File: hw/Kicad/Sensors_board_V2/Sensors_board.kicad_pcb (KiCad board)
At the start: 2 copper layers, 70 x 100 mm, 17 parts, among them J1 SENSORES_LINEA, U1 CNY70, U2 CNY70, U3 CNY70, U4 CNY70, U5 CNY70, U6 CNY70, U7 4053

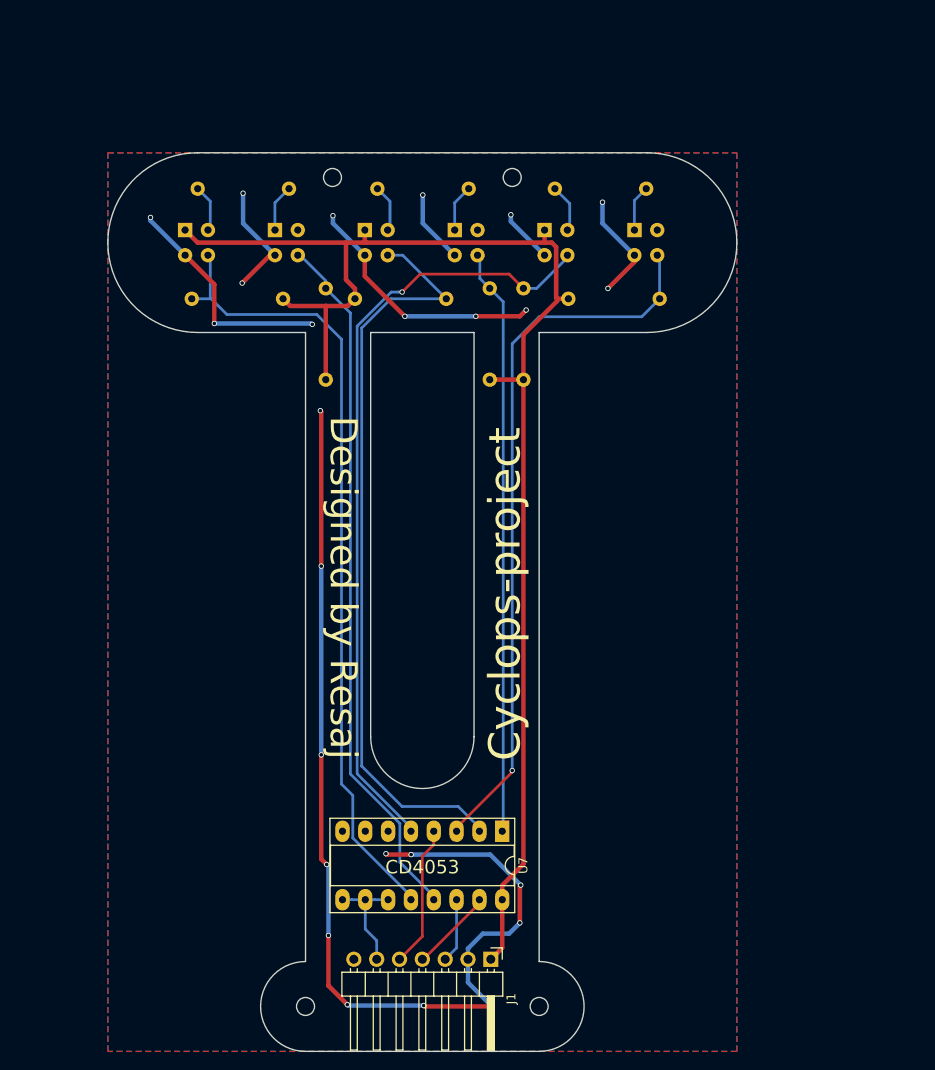
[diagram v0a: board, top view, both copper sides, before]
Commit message: PCB Sensors_board_V2 designed
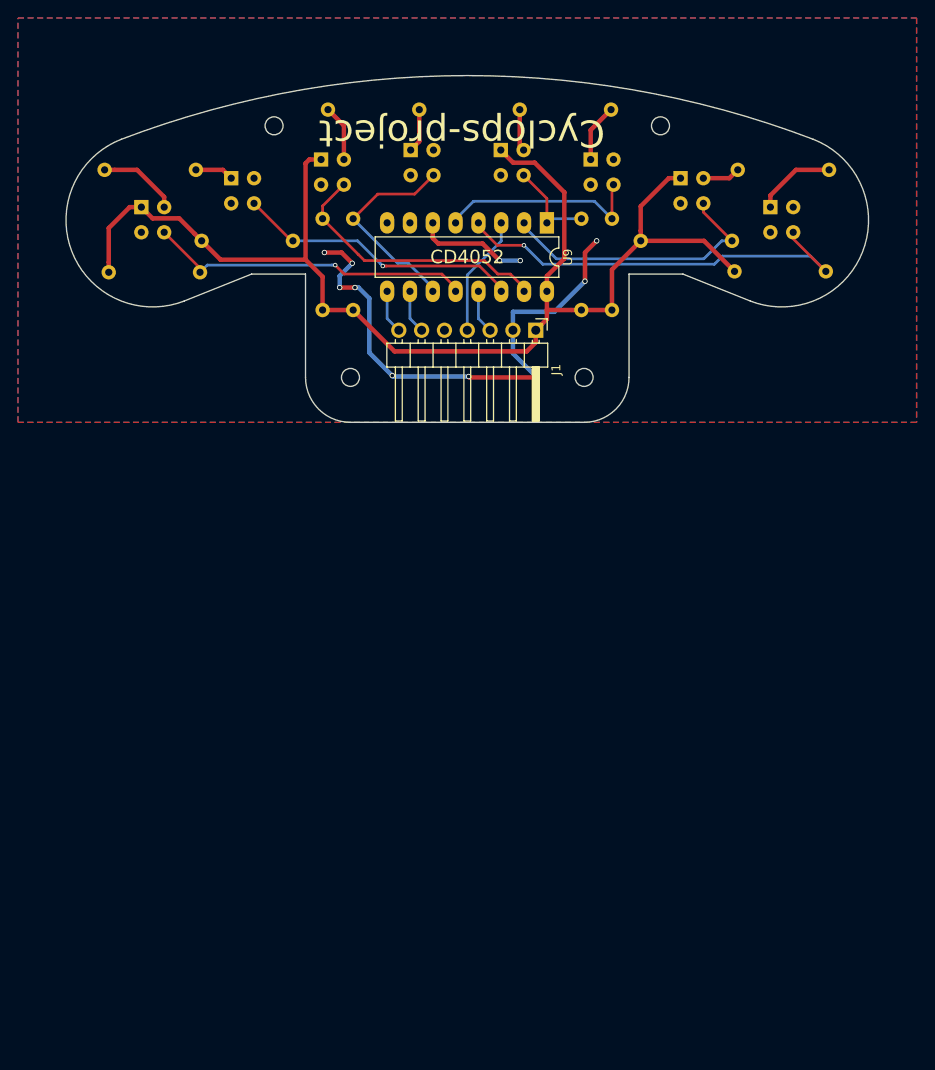
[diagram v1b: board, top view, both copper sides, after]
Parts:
- added R10: 82, Sensors_board:R_Axial_DIN0207_L6.3mm_D2.5mm_P10.16mm_Horizontal, B.Cu at (161.6, 54.4)
- added R11: 10k, Sensors_board:R_Axial_DIN0207_L6.3mm_D2.5mm_P10.16mm_Horizontal, B.Cu at (150.8, 62.3)
- added R12: 10k, Sensors_board:R_Axial_DIN0207_L6.3mm_D2.5mm_P10.16mm_Horizontal, B.Cu at (161.2, 65.7)
- added U8: CNY70, Sensors_board:Vishay_CNY70, B.Cu at (165.2, 58.5)
- added U9: 4052, Package_DIP:DIP-16_W7.62mm_LongPads, F.Cu at (140.4, 60.3)
- U7: value 4053 -> CNY70; footprint Sensors_board:DIP-16_W7.62mm_Socket_LongPads -> Sensors_board:Vishay_CNY70; moved to B.Cu
- moved U7 75.3 mm to (155.2, 55.3)
- moved J1 70.2 mm to (139.1, 72.2)
- moved R3 20.7 mm to (101.9, 62.3), turned to 0 degrees
- moved R2 19.6 mm to (91.6, 65.8), turned to 0 degrees
- moved R6 17.1 mm to (118.8, 70.0)
- moved R1 10.6 mm to (91.1, 54.4)
- moved R4 10.4 mm to (116.0, 47.7)
- moved U4 10.2 mm to (125.2, 52.2)
- moved U5 10.1 mm to (135.2, 52.2)
- moved R8 10.1 mm to (144.2, 70.0)
- moved R7 9.63 mm to (137.3, 47.7)
- moved U6 9.24 mm to (145.2, 53.2)
- moved U3 9.24 mm to (115.2, 53.2)
- moved U2 7.55 mm to (105.2, 55.3)
- moved U1 5.50 mm to (95.2, 58.5)
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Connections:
- J1 pad 5: LINEA_3 -> (no net)
- J1 pad 7: (no net) -> LINEA_SEL_2
- U7 pad 1: SENSOR_4 -> +5V
- U7 pad 2: SENSOR_3 -> Net-(R10-Pad1)
- U7 pad 3: SENSOR_6 -> SENSOR_7
- U7 pad 4: LINEA_3 -> GND
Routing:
- net GND: track 212.5 -> 71.8 mm, vias 25 -> 11
- net SENSOR_5: track 86.9 -> 10.4 mm, vias 1 -> 0
- net SENSOR_6: track 80.1 -> 23.3 mm, vias 1 -> 0
- net SENSOR_3: track 84.1 -> 30.8 mm
- net SENSOR_1: track 89.0 -> 36.3 mm, vias 0 -> 1
- net SENSOR_8: track 0.00 -> 47.7 mm, vias 0 -> 1
- net SENSOR_2: track 77.9 -> 31.8 mm, vias 0 -> 1
- net SENSOR_4: track 65.2 -> 23.4 mm
- net SENSOR_7: track 0.00 -> 31.4 mm
- net +5V: track 155.8 -> 140.0 mm
- net LINEA_3: track 15.8 -> 0.00 mm
- net Net-(R10-Pad2): track 0.00 -> 9.01 mm
- net LINEA_SEL_1: track 12.2 -> 4.87 mm
- net LINEA_SEL_2: track 0.00 -> 4.87 mm
- net Net-(R10-Pad1): track 0.00 -> 4.22 mm
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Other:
- board size 70 x 100 mm -> 89.3 x 38.6 mm
- board text added: "CD4052"
- board text added: "Resaj"
- board text removed: "CD4053"
- board text removed: "Designed by Resaj"
